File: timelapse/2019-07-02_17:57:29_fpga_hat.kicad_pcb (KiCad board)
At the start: 4 copper layers, 65 x 56.5 mm, 90 parts, among them J1 2x20, J2 AudioJack3, J3 Conn_02x06_Top_Bottom, J4 Conn_02x06_Top_Bottom, J5 Conn_02x06_Top_Bottom, J6 Conn_01x02, SW1 PTS815, SW2 PTS815, SW3 PTS815, SW4 PTS815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

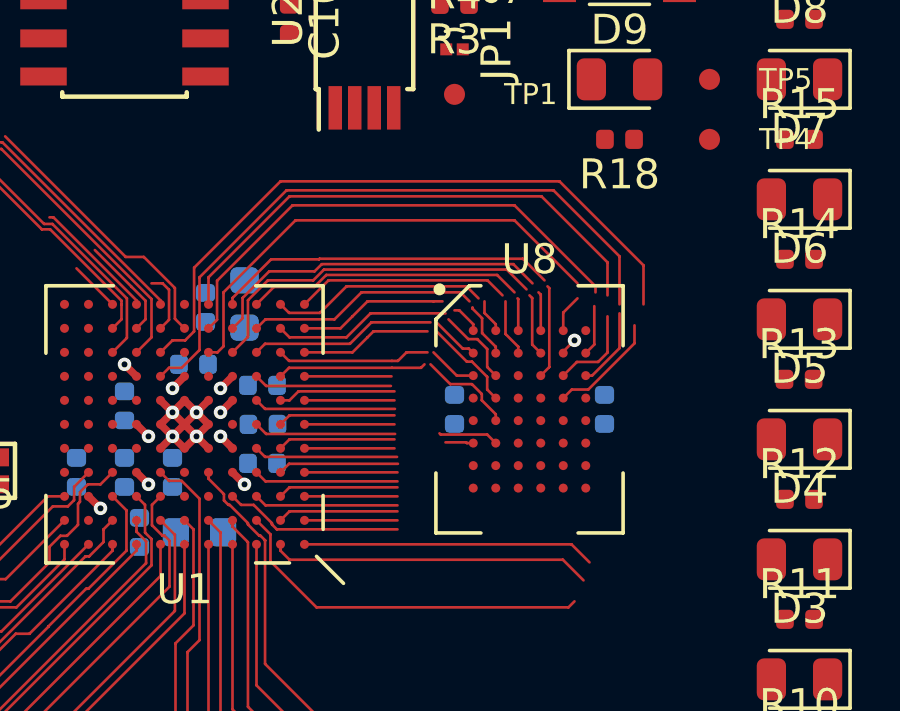
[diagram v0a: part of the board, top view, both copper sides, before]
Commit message: Continue FPGA escape. Start escaping SRAM.
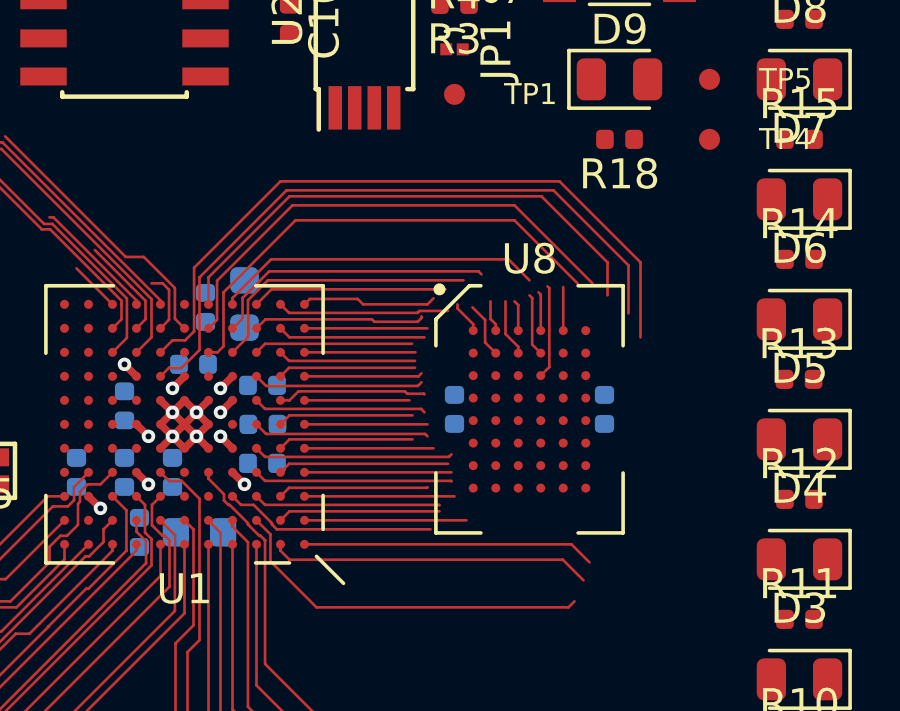
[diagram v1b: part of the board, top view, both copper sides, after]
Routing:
- net /SRAM_A15: track 9.25 -> 6.51 mm
- net /SRAM_DQ11: track 6.14 -> 3.50 mm
- net /SRAM_A10: track 7.14 -> 4.53 mm
- net /SRAM_A14: track 11.9 -> 9.41 mm
- net /SRAM_DQ3: track 8.56 -> 6.22 mm
- net /SRAM_DQ12: track 7.93 -> 5.77 mm
- net /SRAM_DQ10: track 6.63 -> 4.52 mm
- net /SRAM_A17: track 11.5 -> 9.52 mm
- net /SRAM_A13: track 7.72 -> 5.76 mm
- net /SRAM_DQ5: track 3.10 -> 5.00 mm
- net /SRAM_A9: track 4.80 -> 6.65 mm
- net /SRAM_DQ7: track 3.10 -> 4.90 mm
- net /SRAM_DQ1: track 7.02 -> 5.42 mm
- net /SRAM_DQ2: track 8.65 -> 7.08 mm
- net /SRAM_A12: track 7.25 -> 5.72 mm
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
